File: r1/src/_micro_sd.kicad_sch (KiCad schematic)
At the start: 6 parts, among them J4 TF-15x15

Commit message: Assign MPN's and LCSC part numbers
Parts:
- J4: LCSC (none) -> C111196; MPN (none) -> TF-15x15
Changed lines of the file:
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@@
+      (effects (font (size 1.27 1.27)) hide)
+    )
+    (property "LCSC" "C111196" (at 170.18 100.33 0)
+      (effects (font (size 1.27 1.27)) hide)
+    )
+    (property "MPN" "TF-15x15" (at 170.18 100.33 0)
       (effects (font (size 1.27 1.27)) hide)
     )

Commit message: Assign manufacturers
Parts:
- J4: Manufacturer (none) -> SOFNG
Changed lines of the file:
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@@
+      (effects (font (size 1.27 1.27)) hide)
+    )
+    (property "Manufacturer" "SOFNG" (at 170.18 100.33 0)
       (effects (font (size 1.27 1.27)) hide)
     )

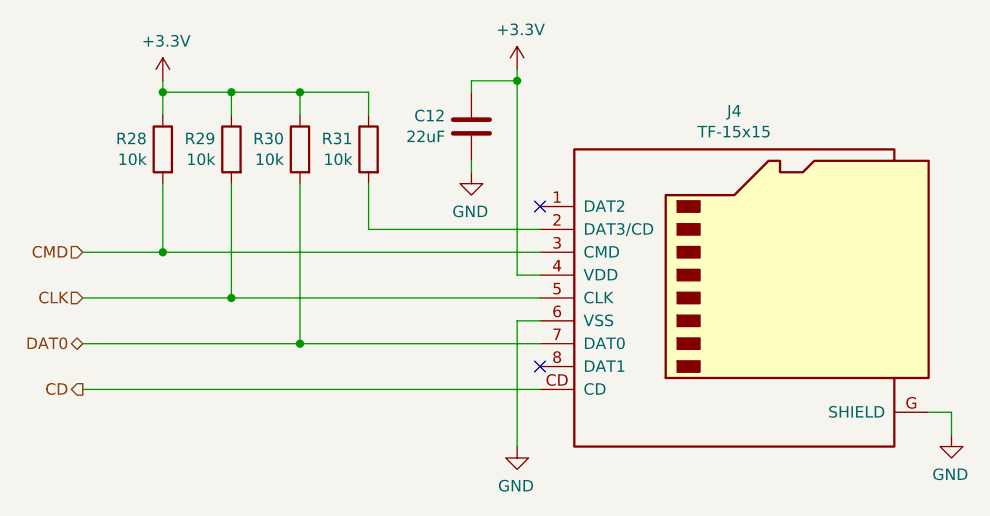
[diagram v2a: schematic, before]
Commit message: Reannotate component refs
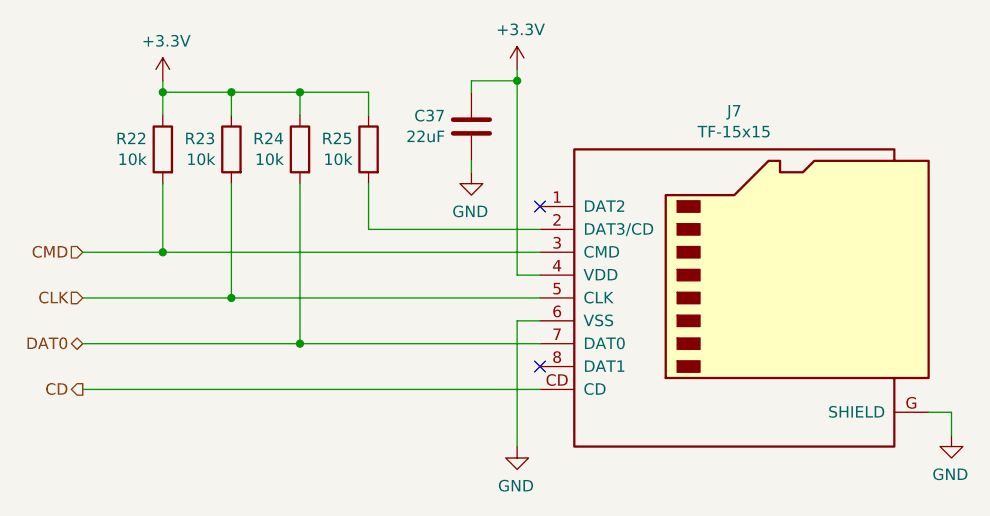
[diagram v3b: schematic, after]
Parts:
- renumbered C12 to C37, J4 to J7, R28 to R22, R29 to R23, R30 to R24, R31 to R25
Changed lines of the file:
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@@
   (symbol (lib_id "j_Connector:Micro_SD_Card_CD") (at 170.18 100.33 0) (unit 1)
     (in_bom yes) (on_board yes) (dnp no)
-    (property "Reference" "J4" (at 168.91 79.5782 0)
+    (property "Reference" "J7" (at 168.91 79.5782 0)
       (effects (font (size 1.27 1.27)))
     )
@@
       (project "tr23-badge-r1"
         (path "/ab725fe7-4504-40ef-b6af-82d065d00fb6/00000000-0000-0000-0000-00005e488944"
-          (reference "J4") (unit 1)
+          (reference "J7") (unit 1)
         )
       )
@@
   (symbol (lib_id "power:GND") (at 193.04 115.57 0) (mirror y) (unit 1)
     (in_bom yes) (on_board yes) (dnp no)
-    (property "Reference" "#PWR053" (at 193.04 121.92 0)
+    (property "Reference" "#PWR079" (at 193.04 121.92 0)
       (effects (font (size 1.27 1.27)) hide)
     )
@@
       (project "tr23-badge-r1"
         (path "/ab725fe7-4504-40ef-b6af-82d065d00fb6/00000000-0000-0000-0000-00005e488944"
-          (reference "#PWR053") (unit 1)
+          (reference "#PWR079") (unit 1)
         )
         (path "/ab725fe7-4504-40ef-b6af-82d065d00fb6"
@@
   (symbol (lib_id "power:GND") (at 144.78 116.84 0) (mirror y) (unit 1)
     (in_bom yes) (on_board yes) (dnp no)
-    (property "Reference" "#PWR052" (at 144.78 123.19 0)
+    (property "Reference" "#PWR078" (at 144.78 123.19 0)
       (effects (font (size 1.27 1.27)) hide)
     )
@@
       (project "tr23-badge-r1"
         (path "/ab725fe7-4504-40ef-b6af-82d065d00fb6/00000000-0000-0000-0000-00005e488944"
-          (reference "#PWR052") (unit 1)
+          (reference "#PWR078") (unit 1)
         )
         (path "/ab725fe7-4504-40ef-b6af-82d065d00fb6"
@@
   (symbol (lib_id "power:+3.3V") (at 144.78 74.93 0) (unit 1)
     (in_bom yes) (on_board yes) (dnp no)
-    (property "Reference" "#PWR051" (at 144.78 78.74 0)
+    (property "Reference" "#PWR077" (at 144.78 78.74 0)
       (effects (font (size 1.27 1.27)) hide)
     )
@@
       (project "tr23-badge-r1"
         (path "/ab725fe7-4504-40ef-b6af-82d065d00fb6/00000000-0000-0000-0000-00005e488944"
-          (reference "#PWR051") (unit 1)
+          (reference "#PWR077") (unit 1)
         )
         (path "/ab725fe7-4504-40ef-b6af-82d065d00fb6"
@@
   (symbol (lib_id "Device:C") (at 139.7 81.28 0) (mirror y) (unit 1)
     (in_bom yes) (on_board yes) (dnp no)
-    (property "Reference" "C12" (at 136.779 80.1116 0)
+    (property "Reference" "C37" (at 136.779 80.1116 0)
       (effects (font (size 1.27 1.27)) (justify left))
     )
@@
       (project "tr23-badge-r1"
         (path "/ab725fe7-4504-40ef-b6af-82d065d00fb6/00000000-0000-0000-0000-00005e488944"
-          (reference "C12") (unit 1)
+          (reference "C37") (unit 1)
         )
         (path "/ab725fe7-4504-40ef-b6af-82d065d00fb6"
@@
   (symbol (lib_id "power:GND") (at 139.7 86.36 0) (mirror y) (unit 1)
     (in_bom yes) (on_board yes) (dnp no)
-    (property "Reference" "#PWR050" (at 139.7 92.71 0)
+    (property "Reference" "#PWR076" (at 139.7 92.71 0)
       (effects (font (size 1.27 1.27)) hide)
     )
@@
       (project "tr23-badge-r1"
         (path "/ab725fe7-4504-40ef-b6af-82d065d00fb6/00000000-0000-0000-0000-00005e488944"
-          (reference "#PWR050") (unit 1)
+          (reference "#PWR076") (unit 1)
         )
         (path "/ab725fe7-4504-40ef-b6af-82d065d00fb6"
@@
   (symbol (lib_id "Device:R") (at 120.65 83.82 0) (mirror y) (unit 1)
     (in_bom yes) (on_board yes) (dnp no)
-    (property "Reference" "R30" (at 118.872 82.6516 0)
+    (property "Reference" "R24" (at 118.872 82.6516 0)
       (effects (font (size 1.27 1.27)) (justify left))
     )
@@
       (project "tr23-badge-r1"
         (path "/ab725fe7-4504-40ef-b6af-82d065d00fb6/00000000-0000-0000-0000-00005e488944"
-          (reference "R30") (unit 1)
+          (reference "R24") (unit 1)
         )
         (path "/ab725fe7-4504-40ef-b6af-82d065d00fb6"
@@
   (symbol (lib_id "Device:R") (at 113.03 83.82 0) (mirror y) (unit 1)
     (in_bom yes) (on_board yes) (dnp no)
-    (property "Reference" "R29" (at 111.252 82.6516 0)
+    (property "Reference" "R23" (at 111.252 82.6516 0)
       (effects (font (size 1.27 1.27)) (justify left))
     )
@@
       (project "tr23-badge-r1"
         (path "/ab725fe7-4504-40ef-b6af-82d065d00fb6/00000000-0000-0000-0000-00005e488944"
-          (reference "R29") (unit 1)
+          (reference "R23") (unit 1)
         )
         (path "/ab725fe7-4504-40ef-b6af-82d065d00fb6"
@@
   (symbol (lib_id "Device:R") (at 105.41 83.82 0) (mirror y) (unit 1)
     (in_bom yes) (on_board yes) (dnp no)
-    (property "Reference" "R28" (at 103.632 82.6516 0)
+    (property "Reference" "R22" (at 103.632 82.6516 0)
       (effects (font (size 1.27 1.27)) (justify left))
     )
@@
       (project "tr23-badge-r1"
         (path "/ab725fe7-4504-40ef-b6af-82d065d00fb6/00000000-0000-0000-0000-00005e488944"
-          (reference "R28") (unit 1)
+          (reference "R22") (unit 1)
         )
         (path "/ab725fe7-4504-40ef-b6af-82d065d00fb6"
@@
   (symbol (lib_id "power:+3.3V") (at 105.41 76.2 0) (unit 1)
     (in_bom yes) (on_board yes) (dnp no)
-    (property "Reference" "#PWR049" (at 105.41 80.01 0)
+    (property "Reference" "#PWR075" (at 105.41 80.01 0)
       (effects (font (size 1.27 1.27)) hide)
     )
@@
       (project "tr23-badge-r1"
         (path "/ab725fe7-4504-40ef-b6af-82d065d00fb6/00000000-0000-0000-0000-00005e488944"
-          (reference "#PWR049") (unit 1)
+          (reference "#PWR075") (unit 1)
         )
         (path "/ab725fe7-4504-40ef-b6af-82d065d00fb6"
@@
   (symbol (lib_id "Device:R") (at 128.27 83.82 0) (mirror y) (unit 1)
     (in_bom yes) (on_board yes) (dnp no)
-    (property "Reference" "R31" (at 126.492 82.6516 0)
+    (property "Reference" "R25" (at 126.492 82.6516 0)
       (effects (font (size 1.27 1.27)) (justify left))
     )
@@
       (project "tr23-badge-r1"
         (path "/ab725fe7-4504-40ef-b6af-82d065d00fb6/00000000-0000-0000-0000-00005e488944"
-          (reference "R31") (unit 1)
-        )
-        (path "/ab725fe7-4504-40ef-b6af-82d065d00fb6"
+          (reference "R25") (unit 1)
+        )
+        (path "/ab725fe7-4504-40ef-b6af-82d065d00fb6"

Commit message: Assign footprints from jeffmakes-footprints lib
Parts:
- J7: footprint jeffmakes-footprints:microSD_HC_Sofng_TF-15 -> jeffmakes_footprints:microSD_HC_Sofng_TF-15
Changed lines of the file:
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@@
       (effects (font (size 1.27 1.27)))
     )
-    (property "Footprint" "jeffmakes-footprints:microSD_HC_Sofng_TF-15" (at 222.25 82.55 0)
+    (property "Footprint" "jeffmakes_footprints:microSD_HC_Sofng_TF-15" (at 222.25 82.55 0)
       (effects (font (size 1.27 1.27)) hide)
     )

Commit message: ERC pass. Schematic complete.
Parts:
- J7: footprint jeffmakes_footprints:microSD_HC_Sofng_TF-15 -> jeffmakes-footprints:microSD_HC_Sofng_TF-15
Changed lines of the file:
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@@
       (effects (font (size 1.27 1.27)))
     )
-    (property "Footprint" "jeffmakes_footprints:microSD_HC_Sofng_TF-15" (at 222.25 82.55 0)
+    (property "Footprint" "jeffmakes-footprints:microSD_HC_Sofng_TF-15" (at 222.25 82.55 0)
       (effects (font (size 1.27 1.27)) hide)
     )
